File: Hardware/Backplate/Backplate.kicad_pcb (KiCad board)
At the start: 2 copper layers, 78 x 27 mm, 5 parts

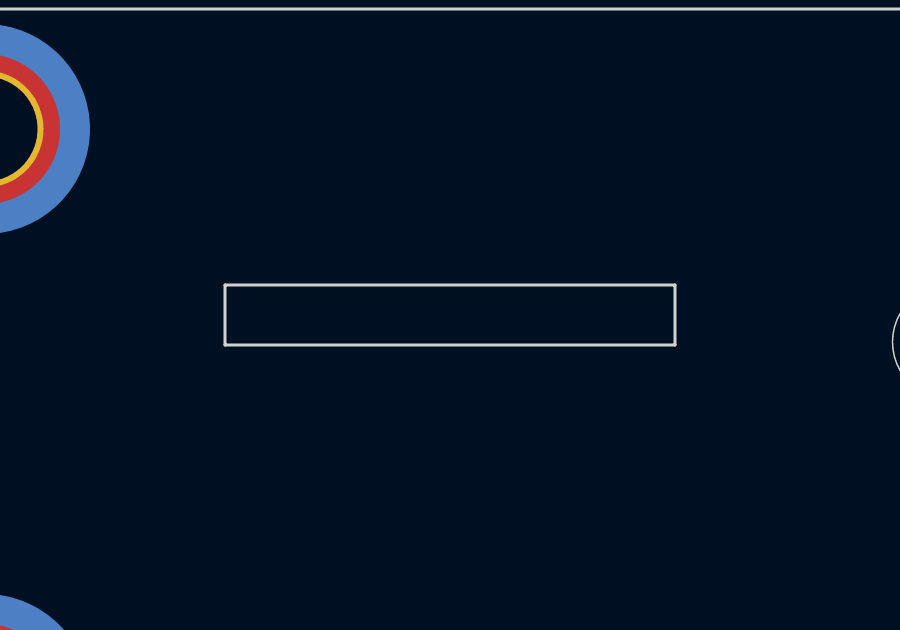
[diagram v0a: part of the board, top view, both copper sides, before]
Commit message: First working version, with 12-lead recording
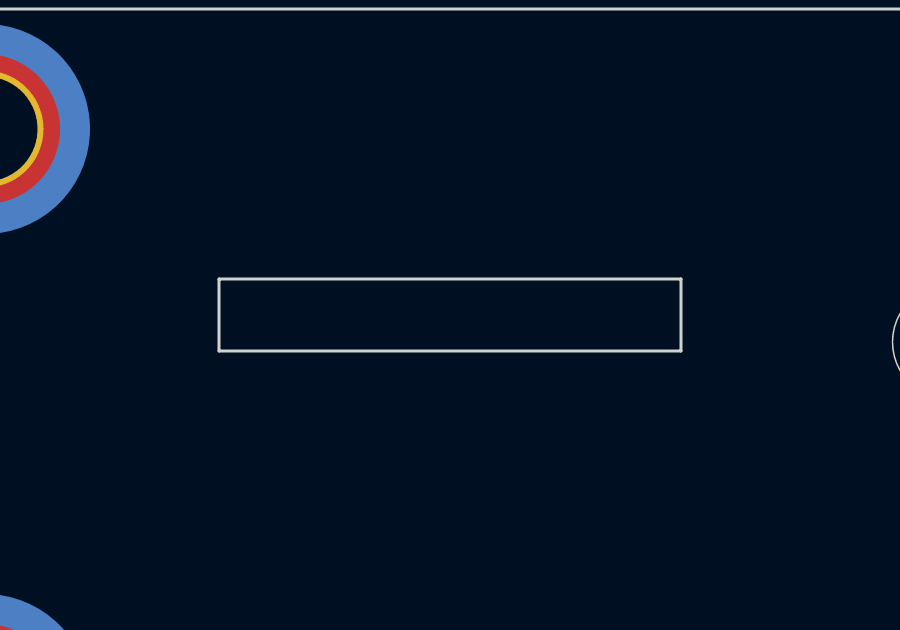
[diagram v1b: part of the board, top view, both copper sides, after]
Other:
- outline, holes or cut-outs redrawn
- board text added: "JLCJLCJLCJLC"
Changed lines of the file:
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@@
       (outputformat 1)
       (mirror false)
-      (drillshape 1)
+      (drillshape 0)
       (scaleselection 1)
-      (outputdirectory "")
+      (outputdirectory "Output/Gerbers")
     )
   )
@@
   (gr_line (start 141.85 115.2) (end 136.15 115.2)
     (stroke (width 0.05) (type solid)) (layer "Edge.Cuts"))
-  (gr_rect (start 112 115.2) (end 127 117.2)
+  (gr_rect (start 111.8 115) (end 127.2 117.4)
     (stroke (width 0.1) (type default)) (fill none) (layer "Edge.Cuts"))
   (gr_line (start 178 110) (end 178 129)
@@
   (gr_line (start 100 115) (end 127 115)
     (stroke (width 0.15) (type default)) (layer "User.9"))
+  (gr_text "JLCJLCJLCJLC" (at 171 132.7) (layer "B.SilkS")
+    (effects (font (size 0.7 0.7) (thickness 0.15)) (justify left bottom mirror))
+  )
   (gr_text "USB" (at 136.1 114.1) (layer "F.Mask")
     (effects (font (face "Futura") (size 2 2) (thickness 0.15)) (justify left bottom))
